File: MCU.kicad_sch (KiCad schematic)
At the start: 1 part, among them U1 ESP32-S3-WROOM-1

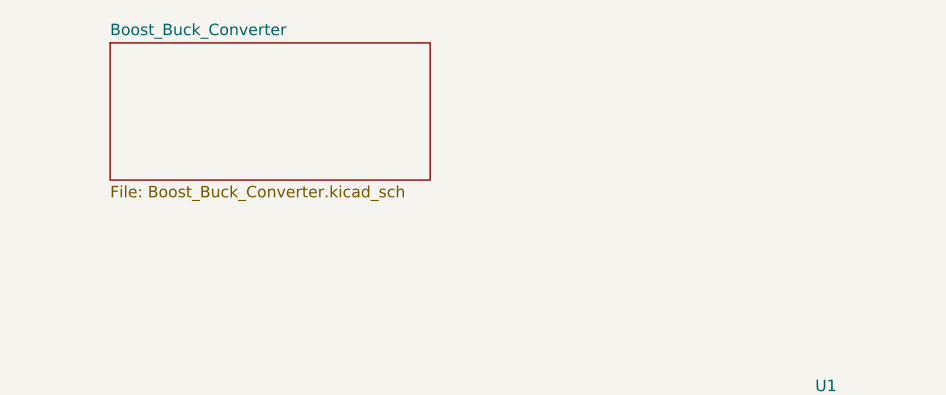
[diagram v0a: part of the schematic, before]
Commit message: add boost-buck converter fixed 3.3V, charger battery Li-on 1S, cut-off circuit's supply. modify gitignore
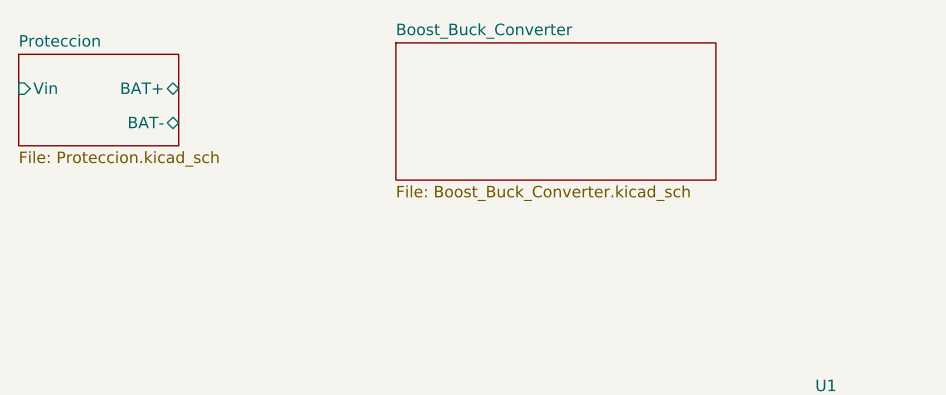
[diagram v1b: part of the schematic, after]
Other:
- added sheet Proteccion (Proteccion.kicad_sch)
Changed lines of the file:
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@@
 		(instances
 			(project "Zicote"
-				(path "/6b0fc6cc-2a24-4473-b451-05b55e127697"
-					(reference "U1")
-					(unit 1)
-				)
 				(path "/6b0fc6cc-2a24-4473-b451-05b55e127697/fad689dd-4fa6-4985-905f-0b15ef4f9b39"
 					(reference "U1")
@@
 	)
 	(sheet
-		(at 36.83 26.67)
+		(at 26.67 27.94)
+		(size 17.78 10.16)
+		(exclude_from_sim no)
+		(in_bom yes)
+		(on_board yes)
+		(dnp no)
+		(fields_autoplaced yes)
+		(stroke
+			(width 0.1524)
+			(type solid)
+		)
+		(fill
+			(color 0 0 0 0)
+		)
+		(property "Sheetname" "Proteccion"
+			(at 26.67 27.2284 0)
+			(show_name no)
+			(do_not_autoplace no)
+			(effects
+				(font
+					(size 1.27 1.27)
+				)
+				(justify left bottom)
+			)
+		)
+		(property "Sheetfile" "Proteccion.kicad_sch"
+			(at 26.67 38.6846 0)
+			(show_name no)
+			(do_not_autoplace no)
+			(effects
+				(font
+					(size 1.27 1.27)
+				)
+				(justify left top)
+			)
+		)
+		(pin "BAT+" bidirectional
+			(at 44.45 31.75 0)
+			(effects
+				(font
+					(size 1.27 1.27)
+				)
+				(justify right)
+			)
+		)
+		(pin "BAT-" bidirectional
+			(at 44.45 35.56 0)
+			(effects
+				(font
+					(size 1.27 1.27)
+				)
+				(justify right)
+			)
+		)
+		(pin "Vin" input
+			(at 26.67 31.75 180)
+			(effects
+				(font
+					(size 1.27 1.27)
+				)
+				(justify left)
+			)
+		)
+		(instances
+			(project "Zicote"
+				(path "/6b0fc6cc-2a24-4473-b451-05b55e127697/fad689dd-4fa6-4985-905f-0b15ef4f9b39"
+					(page "5")
+				)
+			)
+		)
+	)
+	(sheet
+		(at 68.58 26.67)
 		(size 35.56 15.24)
 		(exclude_from_sim no)
@@
 		)
 		(property "Sheetname" "Boost_Buck_Converter"
-			(at 36.83 25.9584 0)
+			(at 68.58 25.9584 0)
 			(show_name no)
 			(do_not_autoplace no)
@@
 		)
 		(property "Sheetfile" "Boost_Buck_Converter.kicad_sch"
-			(at 36.83 42.4946 0)
+			(at 68.58 42.4946 0)
 			(show_name no)
 			(do_not_autoplace no)
